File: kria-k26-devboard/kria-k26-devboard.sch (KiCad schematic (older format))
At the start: 1 part

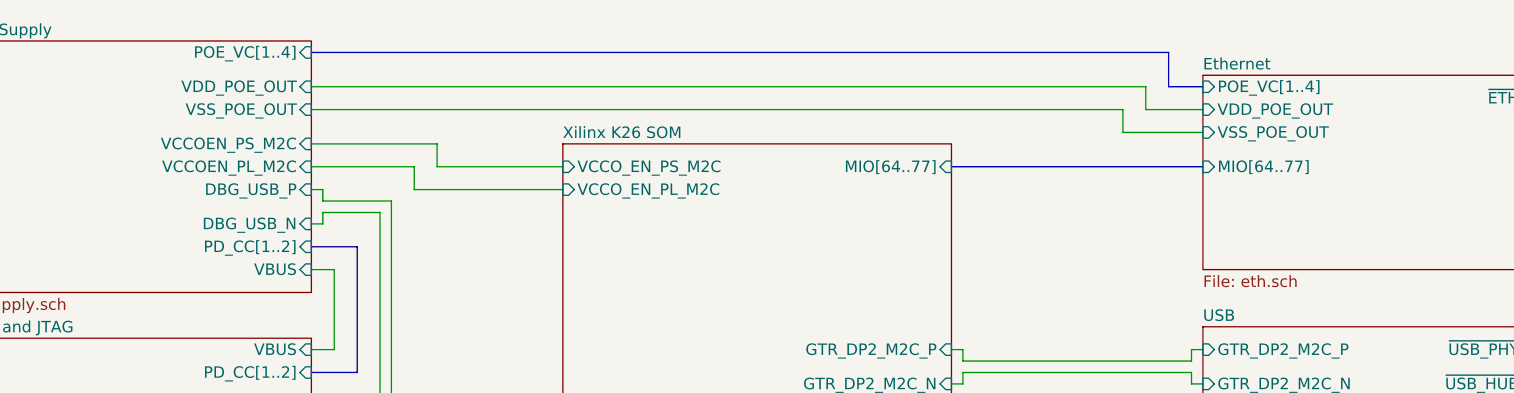
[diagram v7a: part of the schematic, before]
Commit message: Removed PoE PSE and second ETH interface
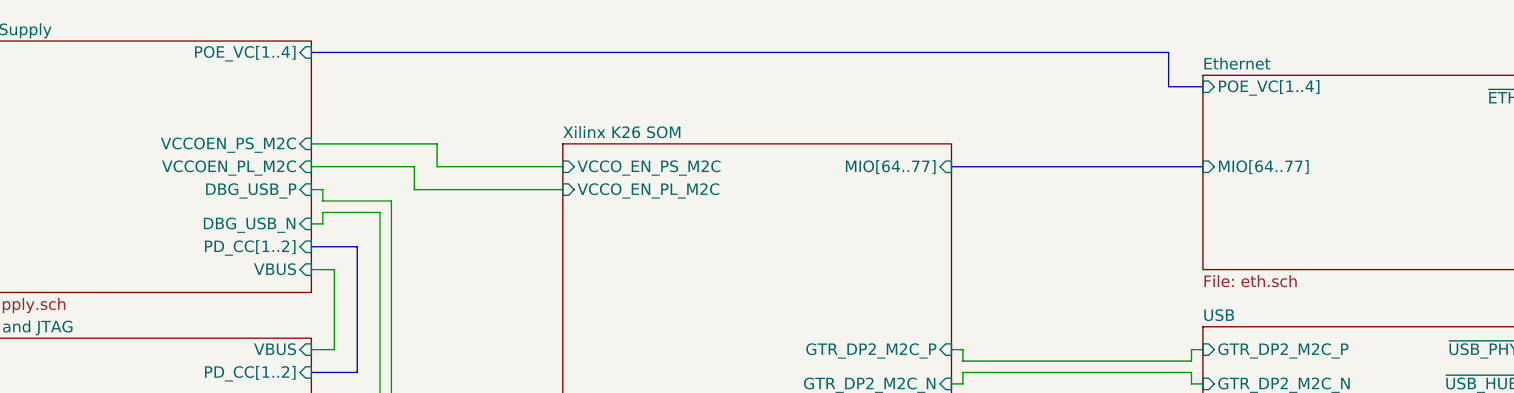
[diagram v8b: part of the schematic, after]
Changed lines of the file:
@@
 F7 "DBG_USB_N" I R 5950 1450 50
 F8 "VBUS" I R 5950 1650 50
-F9 "VDD_POE_OUT" I R 5950 850 50
-F10 "VSS_POE_OUT" I R 5950 950 50
 $EndSheet
 $Sheet
@@
 Wire Bus Line
 	9700 850  9850 850
-Wire Wire Line
-	9850 950  9600 950
-Wire Wire Line
-	9600 950  9600 850
-Wire Wire Line
-	9600 850  5950 850
-Wire Wire Line
-	9850 1050 9500 1050
-Wire Wire Line
-	9500 1050 9500 950
-Wire Wire Line
-	9500 950  5950 950
 $Sheet
 S 9850 1900 1700 900
@@
 F2 "MIO[64..77]" I L 9850 1200 50
 F3 "POE_VC[1..4]" I L 9850 850 50
-F4 "VDD_POE_OUT" I L 9850 950 50
-F5 "VSS_POE_OUT" I L 9850 1050 50
-F6 "~ETH_RESET" I R 11550 900 50
-$EndSheet
-$Sheet
+F4 "~ETH_RESET" I R 11550 900 50
+$EndSheet
+$Sheet
